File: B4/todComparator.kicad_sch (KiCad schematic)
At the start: 0 parts

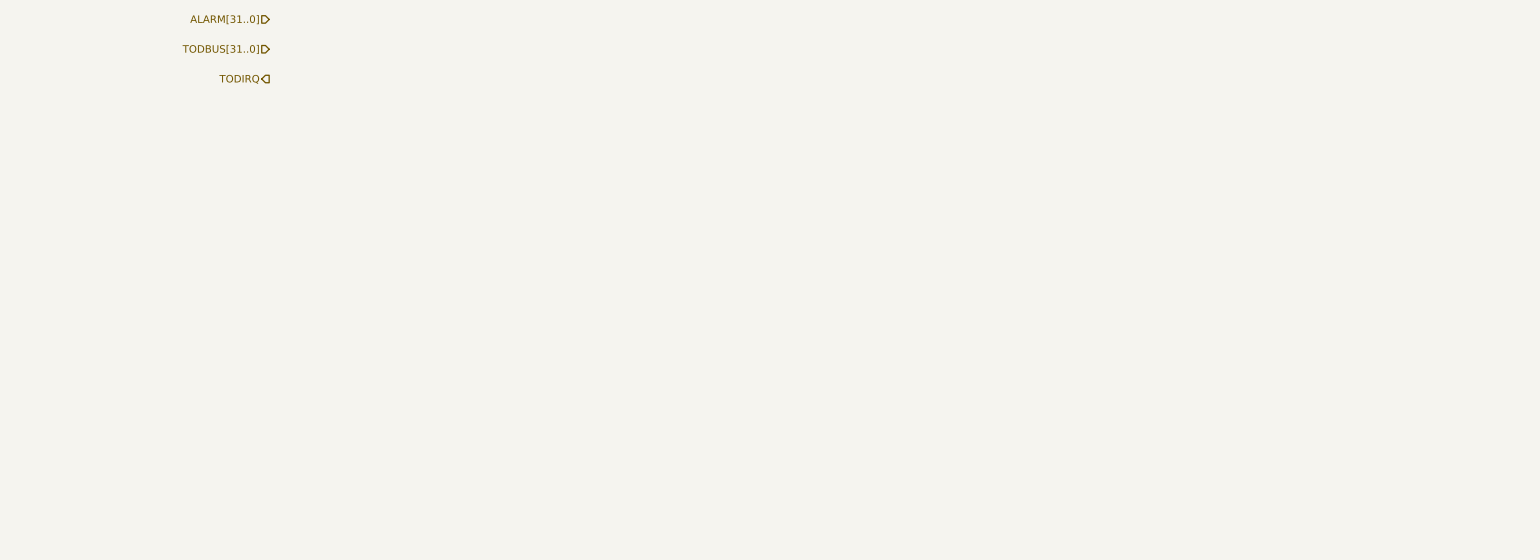
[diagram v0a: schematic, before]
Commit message: B2 refactored. B4 Added. TOD sch completed.
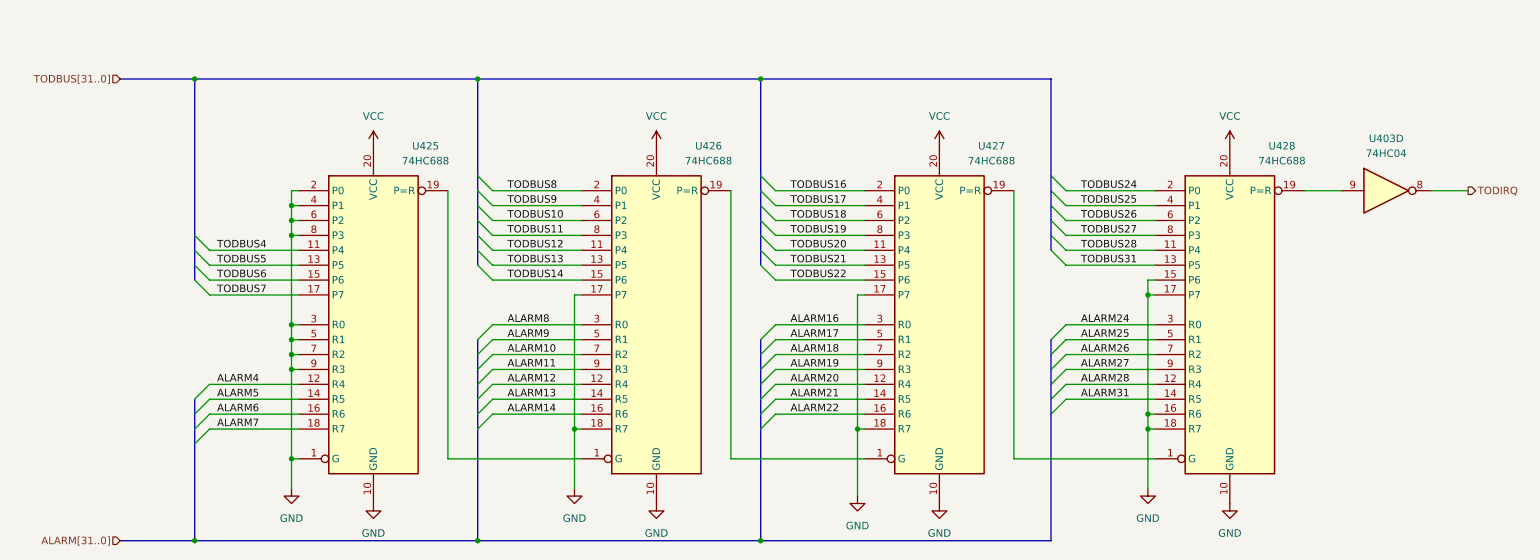
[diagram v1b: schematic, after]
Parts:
- added U403: 74HC04, Package_SO:SOIC-14_3.9x8.7mm_P1.27mm, symbol 74xx:74HC04
- added U425, U426, U427, U428: 74HC688, Package_SO:SOIC-20W_7.5x12.8mm_P1.27mm, symbol 74xx:74HC688
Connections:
- net TODIRQ: now also U403.8
- new net: U427.19 (P=R), U428.1 (G)
- new net: U403.9, U428.19 (P=R)
- new net: U425.19 (P=R), U426.1 (G)
- new net: U426.19 (P=R), U427.1 (G)
- new net ALARM10: U426.7 (R2)
- new net ALARM11: U426.9 (R3)
- new net ALARM12: U426.12 (R4)
- new net ALARM13: U426.14 (R5)
- new net ALARM14: U426.16 (R6)
- new net ALARM16: U427.3 (R0)
- new net ALARM17: U427.5 (R1)
- new net ALARM18: U427.7 (R2)
- new net ALARM19: U427.9 (R3)
- new net ALARM20: U427.12 (R4)
- new net ALARM21: U427.14 (R5)
- new net ALARM22: U427.16 (R6)
- new net ALARM24: U428.3 (R0)
- new net ALARM25: U428.5 (R1)
- new net ALARM26: U428.7 (R2)
- new net ALARM27: U428.9 (R3)
- new net ALARM28: U428.12 (R4)
- new net ALARM31: U428.14 (R5)
- new net ALARM4: U425.12 (R4)
- new net ALARM5: U425.14 (R5)
- new net ALARM6: U425.16 (R6)
- new net ALARM7: U425.18 (R7)
- new net ALARM8: U426.3 (R0)
- new net ALARM9: U426.5 (R1)
- new net GND: U425.1 (G), U425.10 (GND), U425.2 (P0), U425.3 (R0), U425.4 (P1), U425.5 (R1), U425.6 (P2), U425.7 (R2), U425.8 (P3), U425.9 (R3), U426.10 (GND), U426.17 (P7), U426.18 (R7), U427.10 (GND), U427.17 (P7), U427.18 (R7), U428.10 (GND), U428.15 (P6), U428.16 (R6), U428.17 (P7), U428.18 (R7)
- new net TODBUS10: U426.6 (P2)
- new net TODBUS11: U426.8 (P3)
- new net TODBUS12: U426.11 (P4)
- new net TODBUS13: U426.13 (P5)
- new net TODBUS14: U426.15 (P6)
- new net TODBUS16: U427.2 (P0)
- new net TODBUS17: U427.4 (P1)
- new net TODBUS18: U427.6 (P2)
- new net TODBUS19: U427.8 (P3)
- new net TODBUS20: U427.11 (P4)
- new net TODBUS21: U427.13 (P5)
- new net TODBUS22: U427.15 (P6)
- new net TODBUS24: U428.2 (P0)
- new net TODBUS25: U428.4 (P1)
- new net TODBUS26: U428.6 (P2)
- new net TODBUS27: U428.8 (P3)
- new net TODBUS28: U428.11 (P4)
- new net TODBUS31: U428.13 (P5)
- new net TODBUS4: U425.11 (P4)
- new net TODBUS5: U425.13 (P5)
- new net TODBUS6: U425.15 (P6)
- new net TODBUS7: U425.17 (P7)
- new net TODBUS8: U426.2 (P0)
- new net TODBUS9: U426.4 (P1)
- new net VCC: U425.20 (VCC), U426.20 (VCC), U427.20 (VCC), U428.20 (VCC)

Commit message: TOD is here
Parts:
- renumbered U425 to U404, U403 to U503
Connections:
- net ALARM10: now also U426.14 (R5); no longer U426.7 (R2)
- net ALARM11: now also U426.12 (R4); no longer U426.9 (R3)
- net ALARM12: now also U426.16 (R6); no longer U426.12 (R4)
- net ALARM13: now also U426.7 (R2); no longer U426.14 (R5)
- net ALARM14: now also U426.9 (R3); no longer U426.16 (R6)
- net ALARM16: now also U427.5 (R1); no longer U427.3 (R0)
- net ALARM17: now also U427.3 (R0); no longer U427.5 (R1)
- net ALARM18: now also U427.14 (R5); no longer U427.7 (R2)
- net ALARM19: now also U427.12 (R4); no longer U427.9 (R3)
- net ALARM20: now also U427.16 (R6); no longer U427.12 (R4)
- net ALARM21: now also U427.7 (R2); no longer U427.14 (R5)
- net ALARM22: now also U427.9 (R3); no longer U427.16 (R6)
- net ALARM24: now also U428.5 (R1); no longer U428.3 (R0)
- net ALARM25: now also U428.3 (R0); no longer U428.5 (R1)
- net ALARM26: now also U428.14 (R5); no longer U428.7 (R2)
- net ALARM27: now also U428.12 (R4); no longer U428.9 (R3)
- net ALARM28: now also U428.16 (R6); no longer U428.12 (R4)
- net ALARM31: now also U428.18 (R7); no longer U428.14 (R5)
- net ALARM4: now also U404.5 (R1); no longer U404.12 (R4)
- net ALARM5: now also U404.3 (R0); no longer U404.14 (R5)
- net ALARM6: now also U404.14 (R5); no longer U404.16 (R6)
- net ALARM7: now also U404.12 (R4); no longer U404.18 (R7)
- net ALARM8: now also U426.5 (R1); no longer U426.3 (R0)
- net ALARM9: now also U426.3 (R0); no longer U426.5 (R1)
- net GND: now also U404.15 (P6), U404.16 (R6), U404.17 (P7), U404.18 (R7), U428.6 (P2), U428.7 (R2), U428.8 (P3), U428.9 (R3); no longer U404.2 (P0), U404.3 (R0), U404.4 (P1), U404.5 (R1), U428.15 (P6), U428.16 (R6), U428.17 (P7), U428.18 (R7)
- net TODBUS10: now also U426.13 (P5); no longer U426.6 (P2)
- net TODBUS11: now also U426.11 (P4); no longer U426.8 (P3)
- net TODBUS12: now also U426.15 (P6); no longer U426.11 (P4)
- net TODBUS13: now also U426.6 (P2); no longer U426.13 (P5)
- net TODBUS14: now also U426.8 (P3); no longer U426.15 (P6)
- net TODBUS16: now also U427.4 (P1); no longer U427.2 (P0)
- net TODBUS17: now also U427.2 (P0); no longer U427.4 (P1)
- net TODBUS18: now also U427.13 (P5); no longer U427.6 (P2)
- net TODBUS19: now also U427.11 (P4); no longer U427.8 (P3)
- net TODBUS20: now also U427.15 (P6); no longer U427.11 (P4)
- net TODBUS21: now also U427.6 (P2); no longer U427.13 (P5)
- net TODBUS22: now also U427.8 (P3); no longer U427.15 (P6)
- net TODBUS24: now also U428.4 (P1); no longer U428.2 (P0)
- net TODBUS25: now also U428.2 (P0); no longer U428.4 (P1)
- net TODBUS26: now also U428.13 (P5); no longer U428.6 (P2)
- net TODBUS27: now also U428.11 (P4); no longer U428.8 (P3)
- net TODBUS28: now also U428.15 (P6); no longer U428.11 (P4)
- net TODBUS31: now also U428.17 (P7); no longer U428.13 (P5)
- net TODBUS4: now also U404.4 (P1); no longer U404.11 (P4)
- net TODBUS5: now also U404.2 (P0); no longer U404.13 (P5)
- net TODBUS6: now also U404.13 (P5); no longer U404.15 (P6)
- net TODBUS7: now also U404.11 (P4); no longer U404.17 (P7)
- net TODBUS8: now also U426.4 (P1); no longer U426.2 (P0)
- net TODBUS9: now also U426.2 (P0); no longer U426.4 (P1)
- net TODIRQ: now also U503.12; no longer U503.8
- net at U428.19 (P=R): now also U503.13; no longer U503.9

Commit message: Ready for v0.2.2
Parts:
- renumbered U404 to U405, U426 to U411, U427 to U416, U428 to U423, U503 to U429
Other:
- company: (none) -> Daniel Molina
- title: (none) -> 74HCT6526 Board 4
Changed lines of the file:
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@@
 (kicad_sch (version 20211123) (generator eeschema)
   (paper "A4")
+  (title_block
+    (title "74HCT6526 Board 4")
+    (date "2023-06-22")
+    (rev "0.2.2")
+    (company "Daniel Molina")
+    (comment 1 "https://github.com/dmolinagarcia/74HCT6526")
+  )
   (junction (at 53.34 53.34) (diameter 0) (color 0 0 0 0)
   )
@@
   (symbol (lib_id "74xx:74HC688") (at 229.87 95.25 0) (unit 1)
     (in_bom yes) (on_board yes)
-    (property "Reference" "U428" (id 0) (at 238.76 64.77 0))
+    (property "Reference" "U423" (id 0) (at 238.76 64.77 0))
     (property "Value" "74HC688" (id 1) (at 238.76 67.31 0))
     (property "Footprint" "Package_SO:SOIC-20W_7.5x12.8mm_P1.27mm" (id 2) (at 229.87 95.25 0)
@@
   (symbol (lib_id "74xx:74HC688") (at 83.82 95.25 0) (unit 1)
     (in_bom yes) (on_board yes)
-    (property "Reference" "U404" (id 0) (at 92.71 64.77 0))
+    (property "Reference" "U405" (id 0) (at 92.71 64.77 0))
     (property "Value" "74HC688" (id 1) (at 92.71 67.31 0))
     (property "Footprint" "Package_SO:SOIC-20W_7.5x12.8mm_P1.27mm" (id 2) (at 83.82 95.25 0)
@@
   (symbol (lib_id "74xx:74HC04") (at 256.54 72.39 0) (unit 6)
     (in_bom yes) (on_board yes) (fields_autoplaced)
-    (property "Reference" "U503" (id 0) (at 256.54 63.5 0))
+    (property "Reference" "U429" (id 0) (at 256.54 63.5 0))
     (property "Value" "74HC04" (id 1) (at 256.54 66.04 0))
     (property "Footprint" "Package_SO:SOIC-14_3.9x8.7mm_P1.27mm" (id 2) (at 256.54 72.39 0)
@@
   (symbol (lib_id "74xx:74HC688") (at 132.08 95.25 0) (unit 1)
     (in_bom yes) (on_board yes)
-    (property "Reference" "U426" (id 0) (at 140.97 64.77 0))
+    (property "Reference" "U411" (id 0) (at 140.97 64.77 0))
     (property "Value" "74HC688" (id 1) (at 140.97 67.31 0))
     (property "Footprint" "Package_SO:SOIC-20W_7.5x12.8mm_P1.27mm" (id 2) (at 132.08 95.25 0)
@@
   (symbol (lib_id "74xx:74HC688") (at 180.34 95.25 0) (unit 1)
     (in_bom yes) (on_board yes)
-    (property "Reference" "U427" (id 0) (at 189.23 64.77 0))
+    (property "Reference" "U416" (id 0) (at 189.23 64.77 0))
     (property "Value" "74HC688" (id 1) (at 189.23 67.31 0))
     (property "Footprint" "Package_SO:SOIC-20W_7.5x12.8mm_P1.27mm" (id 2) (at 180.34 95.25 0)
